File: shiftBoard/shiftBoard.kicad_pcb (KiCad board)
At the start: 2 copper layers, 29 parts, among them J1 Screw_Terminal_01x02, J2 Screw_Terminal_01x02, J3 Screw_Terminal_01x02, J4 Screw_Terminal_01x02, Q1 AO3400A, Q2 AO3400A, Q3 AO3400A, Q4 AO3400A, Q5 AO3400A, Q6 AO3400A, Q7 AO3400A, Q9 AO3400A, U2 74HC595

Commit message: PCB upgade
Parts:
- moved +12V8 51.0 mm to (175.0, 136.5), turned to 90 degrees
- moved +12V7 44.0 mm to (175.0, 33.5), turned to 90 degrees
- moved Q9 39.8 mm to (145.8, 137.6), turned to 0 degrees
- moved D1 37.5 mm to (155.9, 131.5)
- moved +12V1 34.0 mm to (175.0, 121.5), turned to 90 degrees
- moved D8 32.2 mm to (156.8, 27.5), turned to 0 degrees
- moved +12V6 30.5 mm to (175.0, 47.5), turned to 90 degrees
- moved Q7 25.9 mm to (145.8, 35.0), turned to 0 degrees
- moved Q1 20.2 mm to (145.8, 123.0), turned to 0 degrees
- moved D2 17.4 mm to (155.4, 116.0)
- moved D7 12.2 mm to (156.4, 41.5), turned to 0 degrees
- moved D4 11.7 mm to (156.0, 85.5), turned to 0 degrees
- moved D3 11.4 mm to (155.9, 100.5), turned to 0 degrees
- moved D6 11.4 mm to (156.4, 57.0), turned to 0 degrees
- moved Q2 11.0 mm to (145.8, 107.0)
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
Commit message: PCB board
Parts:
- moved J1 28.9 mm to (125.0, 96.5)
- moved J2 22.2 mm to (125.0, 83.0)
- moved Q9 18.2 mm to (157.0, 123.2), turned to 90 degrees
- moved J3 17.4 mm to (125.0, 69.5)
- moved Q1 16.7 mm to (157.0, 110.7), turned to 90 degrees
- moved J4 16.4 mm to (124.7, 51.0)
- moved Q2 14.1 mm to (157.0, 98.5), turned to 90 degrees
- moved +12V8 13.5 mm to (175.5, 123.0)
- moved D1 13.5 mm to (156.4, 118.0)
- moved Q3 12.7 mm to (157.0, 86.7), turned to 90 degrees
- moved Q4 11.8 mm to (157.0, 74.5), turned to 90 degrees
- moved Q7 11.8 mm to (157.0, 38.5), turned to 90 degrees
- moved Q5 11.4 mm to (157.0, 62.2), turned to 90 degrees
- moved Q6 11.3 mm to (157.0, 50.5), turned to 90 degrees
- moved +12V1 10.5 mm to (175.5, 111.0)
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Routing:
- net Net-(+12V1-Pin_2): track 0.00 -> 90.7 mm
- net Net-(U2-QA): track 0.00 -> 56.8 mm
- net Net-(U2-QB): track 0.00 -> 36.6 mm
- net Net-(U2-QH): track 0.00 -> 35.7 mm
- net Net-(U2-QG): track 0.00 -> 26.4 mm
- net Net-(U2-QC): track 0.00 -> 26.3 mm
- net Net-(+12V7-Pin_1): track 0.00 -> 23.6 mm
- net Net-(+12V1-Pin_1): track 0.00 -> 23.6 mm
- net Net-(+12V6-Pin_1): track 0.00 -> 23.5 mm
- net Net-(+12V5-Pin_1): track 0.00 -> 23.4 mm
- net Net-(+12V3-Pin_1): track 0.00 -> 23.3 mm
- net Net-(+12V2-Pin_1): track 0.00 -> 23.2 mm
- net Net-(+12V8-Pin_1): track 0.00 -> 23.1 mm
- net Net-(+12V4-Pin_1): track 0.00 -> 23.0 mm
- net Net-(U2-QF): track 0.00 -> 16.1 mm
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
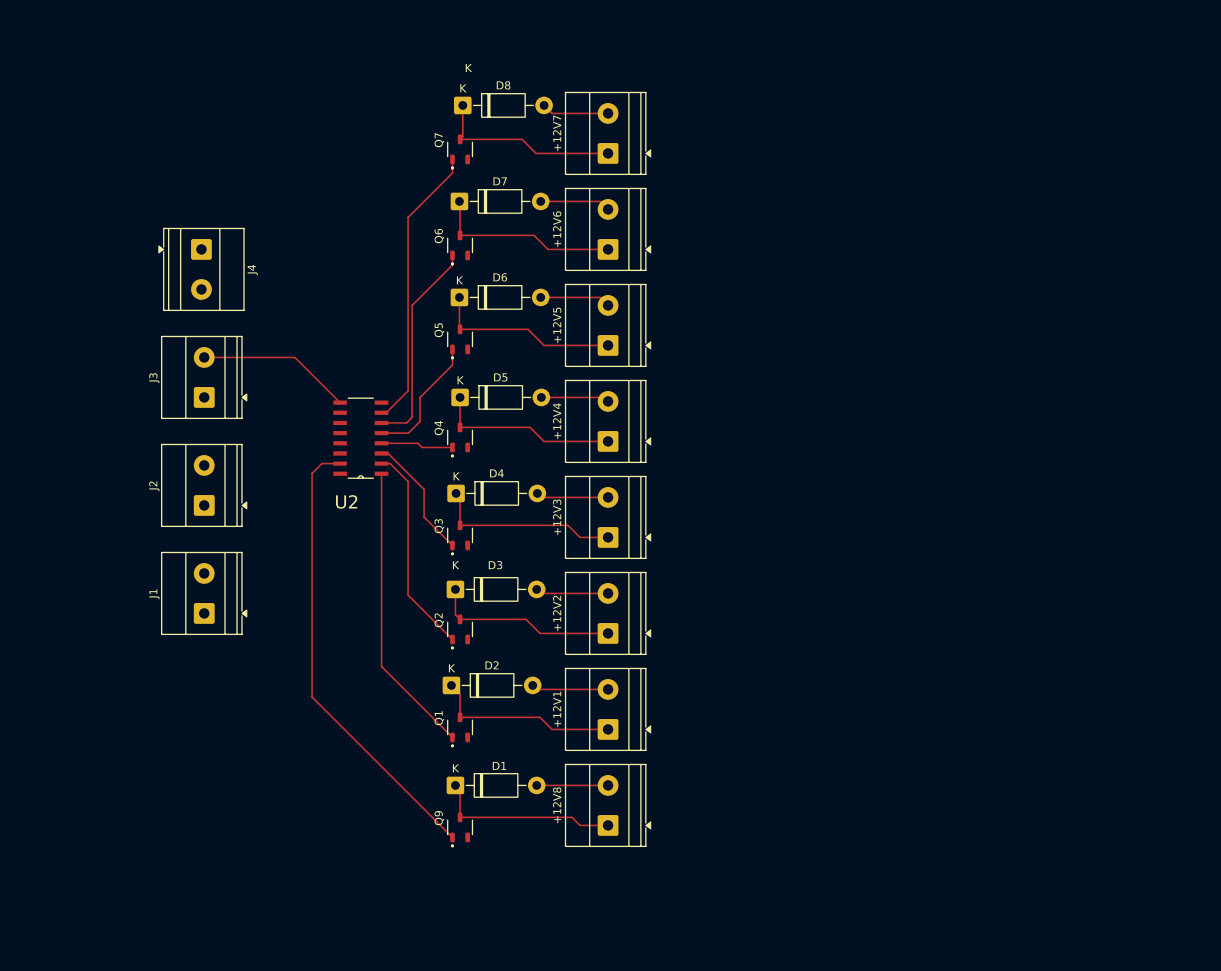
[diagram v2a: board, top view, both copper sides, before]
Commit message: Designed PCB board from scematic
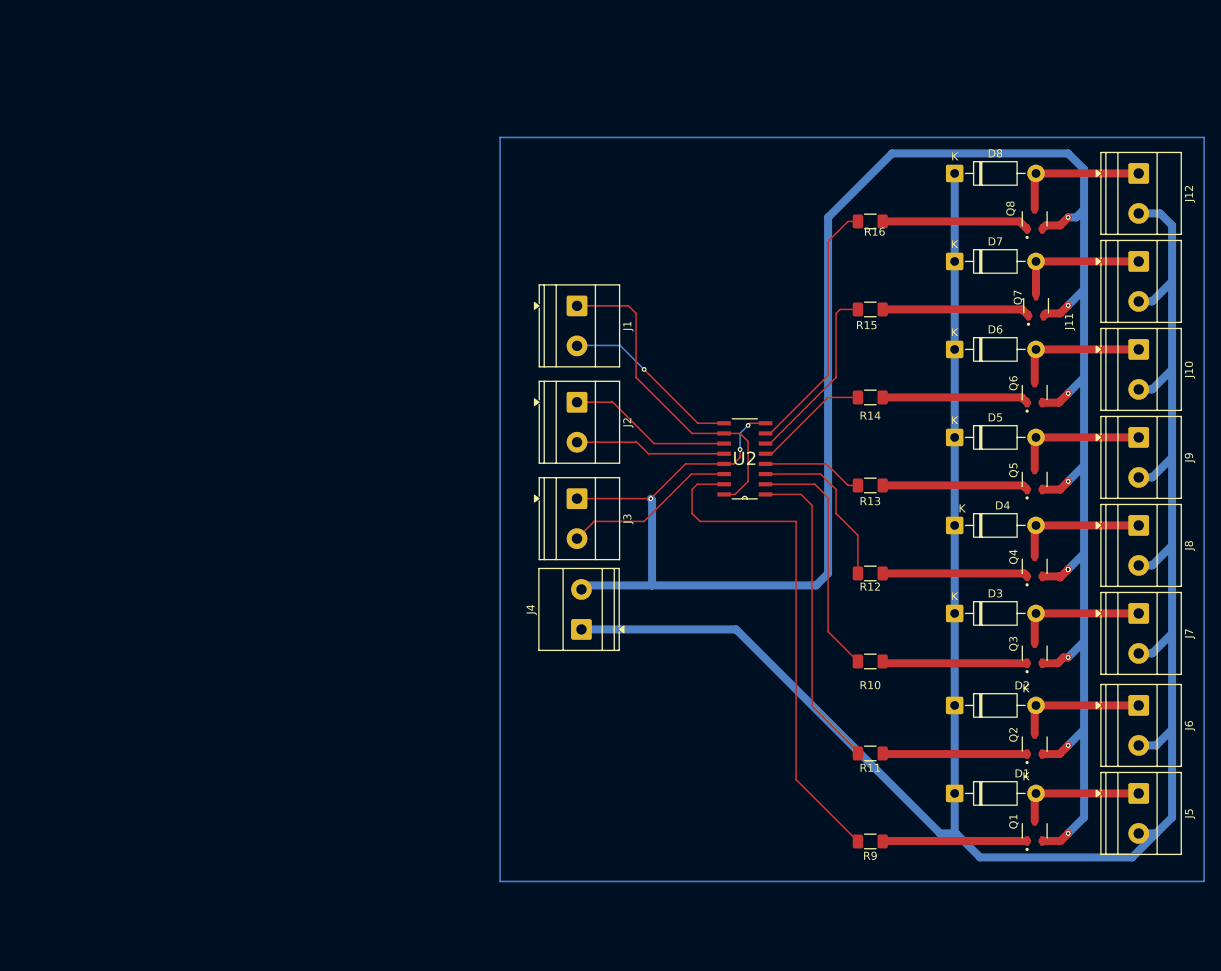
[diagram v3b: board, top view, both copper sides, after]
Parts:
- removed +12V1, +12V2, +12V3, +12V4, +12V5, +12V6, +12V7, +12V8: GND, TerminalBlock_Phoenix:TerminalBlock_Phoenix_MKDS-1,5-2_1x02_P5.00mm_Horizontal
- removed Q9: AO3400A, Library:AO3400A
- added J10: Screw_Terminal_01x02, TerminalBlock_Phoenix:TerminalBlock_Phoenix_MKDS-1,5-2_1x02_P5.00mm_Horizontal, F.Cu at (241.8, 63.5)
- added J11: Screw_Terminal_01x02, TerminalBlock_Phoenix:TerminalBlock_Phoenix_MKDS-1,5-2_1x02_P5.00mm_Horizontal, F.Cu at (241.8, 52.5)
- added J12: Screw_Terminal_01x02, TerminalBlock_Phoenix:TerminalBlock_Phoenix_MKDS-1,5-2_1x02_P5.00mm_Horizontal, F.Cu at (241.8, 41.5)
- added J5: Screw_Terminal_01x02, TerminalBlock_Phoenix:TerminalBlock_Phoenix_MKDS-1,5-2_1x02_P5.00mm_Horizontal, F.Cu at (241.8, 119.0)
- added J6: Screw_Terminal_01x02, TerminalBlock_Phoenix:TerminalBlock_Phoenix_MKDS-1,5-2_1x02_P5.00mm_Horizontal, F.Cu at (241.8, 108.0)
- added J7: Screw_Terminal_01x02, TerminalBlock_Phoenix:TerminalBlock_Phoenix_MKDS-1,5-2_1x02_P5.00mm_Horizontal, F.Cu at (241.8, 96.5)
- added J8: Screw_Terminal_01x02, TerminalBlock_Phoenix:TerminalBlock_Phoenix_MKDS-1,5-2_1x02_P5.00mm_Horizontal, F.Cu at (241.8, 85.5)
- added J9: Screw_Terminal_01x02, TerminalBlock_Phoenix:TerminalBlock_Phoenix_MKDS-1,5-2_1x02_P5.00mm_Horizontal, F.Cu at (241.8, 74.5)
- added Q8: AO3400A, Library:AO3400A, F.Cu at (228.8, 47.2)
- added R10: 100, Resistor_SMD:R_1206_3216Metric_Pad1.30x1.75mm_HandSolder, F.Cu at (208.3, 102.5)
- added R11: 100, Resistor_SMD:R_1206_3216Metric_Pad1.30x1.75mm_HandSolder, F.Cu at (208.3, 114.0)
- added R12: 100, Resistor_SMD:R_1206_3216Metric_Pad1.30x1.75mm_HandSolder, F.Cu at (208.3, 91.5)
- added R13: 100, Resistor_SMD:R_1206_3216Metric_Pad1.30x1.75mm_HandSolder, F.Cu at (208.3, 80.5)
- added R14: 100, Resistor_SMD:R_1206_3216Metric_Pad1.30x1.75mm_HandSolder, F.Cu at (208.3, 69.5)
- added R15: 100, Resistor_SMD:R_1206_3216Metric_Pad1.30x1.75mm_HandSolder, F.Cu at (208.3, 58.5)
- added R16: 100, Resistor_SMD:R_1206_3216Metric_Pad1.30x1.75mm_HandSolder, F.Cu at (208.3, 47.5)
- added R9: 100, Resistor_SMD:R_1206_3216Metric_Pad1.30x1.75mm_HandSolder, F.Cu at (208.3, 125.0)
- moved Q7 74.6 mm to (229.0, 58.0)
- moved Q6 74.1 mm to (228.8, 68.9)
- moved Q5 73.9 mm to (228.8, 79.8)
- moved Q4 73.6 mm to (228.8, 90.6)
- moved Q3 73.3 mm to (228.8, 101.5)
- moved Q2 73.2 mm to (228.8, 112.8)
- moved Q1 73.0 mm to (228.8, 123.7)
- moved J4 67.2 mm to (172.2, 98.5), turned to 90 degrees
- moved D2 63.0 mm to (218.8, 108.0)
- moved D3 62.5 mm to (218.8, 96.5)
- moved D4 62.5 mm to (218.8, 85.5)
- moved D1 62.4 mm to (218.8, 119.0)
- moved D7 62.4 mm to (218.8, 52.5)
- moved D6 62.2 mm to (218.8, 63.5)
- moved D8 62.1 mm to (218.8, 41.5)
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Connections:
- D1 pad 1: Net-(+12V8-Pin_1) -> Net-(D1-K)
- D1 pad 2: Net-(+12V1-Pin_2) -> Net-(D1-A)
- D2 pad 1: Net-(+12V1-Pin_1) -> Net-(D1-K)
- D2 pad 2: Net-(+12V1-Pin_2) -> Net-(D2-A)
- D3 pad 1: Net-(+12V2-Pin_1) -> Net-(D1-K)
- D3 pad 2: Net-(+12V1-Pin_2) -> Net-(D3-A)
- D4 pad 1: Net-(+12V3-Pin_1) -> Net-(D1-K)
- D4 pad 2: Net-(+12V1-Pin_2) -> Net-(D4-A)
- D5 pad 1: Net-(+12V4-Pin_1) -> Net-(D1-K)
- D5 pad 2: Net-(+12V1-Pin_2) -> Net-(D5-A)
- D6 pad 1: Net-(+12V5-Pin_1) -> Net-(D1-K)
- D6 pad 2: Net-(+12V1-Pin_2) -> Net-(D6-A)
- D7 pad 1: Net-(+12V6-Pin_1) -> Net-(D1-K)
- D7 pad 2: Net-(+12V1-Pin_2) -> Net-(D7-A)
- D8 pad 1: Net-(+12V7-Pin_1) -> Net-(D1-K)
- D8 pad 2: Net-(+12V1-Pin_2) -> Net-(D8-A)
- J3 pad 2: Net-(+12V1-Pin_2) -> Net-(J3-Pin_2)
- J4 pad 1: Net-(+12V1-Pin_2) -> Net-(D1-K)
- J4 pad 2: Net-(J4-Pin_2) -> Net-(J3-Pin_1)
- Q1 pad 1: Net-(U2-QB) -> Net-(Q1-Pad1)
- Q1 pad 2: Net-(J4-Pin_2) -> Net-(J3-Pin_1)
- Q1 pad 3: Net-(+12V1-Pin_1) -> Net-(D1-A)
- Q2 pad 1: Net-(U2-QC) -> Net-(Q2-Pad1)
- Q2 pad 2: Net-(J4-Pin_2) -> Net-(J3-Pin_1)
- Q2 pad 3: Net-(+12V2-Pin_1) -> Net-(D2-A)
- Q3 pad 1: Net-(U2-QD) -> Net-(Q3-Pad1)
- Q3 pad 2: Net-(J4-Pin_2) -> Net-(J3-Pin_1)
- Q3 pad 3: Net-(+12V3-Pin_1) -> Net-(D3-A)
- Q4 pad 1: Net-(U2-QE) -> Net-(Q4-Pad1)
- Q4 pad 2: Net-(J4-Pin_2) -> Net-(J3-Pin_1)
- Q4 pad 3: Net-(+12V4-Pin_1) -> Net-(D4-A)
- Q5 pad 1: Net-(U2-QF) -> Net-(Q5-Pad1)
- Q5 pad 2: Net-(J4-Pin_2) -> Net-(J3-Pin_1)
- Q5 pad 3: Net-(+12V5-Pin_1) -> Net-(D5-A)
- Q6 pad 1: Net-(U2-QG) -> Net-(Q6-Pad1)
- Q6 pad 2: Net-(J4-Pin_2) -> Net-(J3-Pin_1)
- Q6 pad 3: Net-(+12V6-Pin_1) -> Net-(D6-A)
- Q7 pad 1: Net-(U2-QH) -> Net-(Q7-Pad1)
- Q7 pad 2: Net-(J4-Pin_2) -> Net-(J3-Pin_1)
- Q7 pad 3: Net-(+12V7-Pin_1) -> Net-(D7-A)
- U2 pad 14: Net-(J1-Pin_2) -> Net-(J3-Pin_2)
- U2 pad 9: Net-(+12V1-Pin_2) -> Net-(J1-Pin_2)
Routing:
- net Net-(J3-Pin_1): track 0.00 -> 284.9 mm, vias 0 -> 12
- net Net-(D1-K): track 0.00 -> 282.3 mm
- net Net-(+12V1-Pin_2): track 90.7 -> 0.00 mm
- net Net-(J1-Pin_1): track 0.00 -> 41.8 mm
- net Net-(+12V7-Pin_1): track 23.6 -> 0.00 mm
- net Net-(+12V1-Pin_1): track 23.6 -> 0.00 mm
- net Net-(+12V6-Pin_1): track 23.5 -> 0.00 mm
- net Net-(+12V5-Pin_1): track 23.4 -> 0.00 mm
- net Net-(+12V3-Pin_1): track 23.3 -> 0.00 mm
- net Net-(+12V2-Pin_1): track 23.2 -> 0.00 mm
- net Net-(+12V8-Pin_1): track 23.1 -> 0.00 mm
- net Net-(+12V4-Pin_1): track 23.0 -> 0.00 mm
- net Net-(J1-Pin_2): track 0.00 -> 22.4 mm, vias 0 -> 1
- net Net-(J3-Pin_2): track 0.00 -> 21.7 mm
- net Net-(J2-Pin_1): track 0.00 -> 20.6 mm
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
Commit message: PCB cut out and errors
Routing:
- net Net-(J3-Pin_1): vias 12 -> 11
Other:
- board outline added: 88 x 93 mm
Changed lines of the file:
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@@
 		(tags "Diode DO-41_SOD81 series Axial Horizontal pin pitch 10.16mm  length 5.2mm diameter 2.7mm")
 		(property "Reference" "D2"
-			(at 8.433809 -2.47 0)
+			(at 5.6725 -2.47 0)
 			(layer "F.SilkS")
 			(effects
@@
 		(tags "Diode DO-41_SOD81 series Axial Horizontal pin pitch 10.16mm  length 5.2mm diameter 2.7mm")
 		(property "Reference" "D1"
-			(at 8.433809 -2.47 0)
+			(at 5.6725 -2.47 0)
 			(layer "F.SilkS")
 			(effects
@@
 		(tags "resistor handsolder")
 		(property "Reference" "R16"
-			(at -0.55 -1.31 0)
+			(at -0.2225 -2 0)
 			(layer "F.SilkS")
 			(effects
@@
 		(stroke
 			(width 0.2)
-			(type default)
+			(type solid)
 		)
 		(fill no)
-		(layer "B.Cu")
+		(layer "Edge.Cuts")
 	)
 	(dimension
@@
 		(size 0.6)
 		(drill 0.3)
-		(layers "F.Cu" "B.Cu")
-		(net 5)
-	)
-	(via
-		(at 233 91)
-		(size 0.6)
-		(drill 0.3)

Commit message: turned a terminal
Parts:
- moved J4 5.05 mm to (171.5, 93.5), turned to -90 degrees
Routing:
- net Net-(D1-K): track 282.3 -> 288.2 mm, vias 0 -> 3
- net Net-(J3-Pin_1): track 284.9 -> 289.4 mm
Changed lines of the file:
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@@
 	(footprint "TerminalBlock_Phoenix:TerminalBlock_Phoenix_MKDS-1,5-2_1x02_P5.00mm_Horizontal"
 		(layer "F.Cu")
-		(at 172.1725 98.5 90)
+		(at 171.5 93.5 -90)
 		(descr "Terminal Block Phoenix MKDS-1,5-2, 2 pins, pitch 5mm, size 10x9.8mm, drill diameter 1.3mm, pad diameter 2.6mm, http://www.farnell.com/datasheets/100425.pdf, script-generated using https://gitlab.com/kicad/libraries/kicad-footprint-generator/-/tree/master/scripts/TerminalBlock_Phoenix")
 		(tags "THT Terminal Block Phoenix MKDS-1,5-2 pitch 5mm size 10x9.8mm drill 1.3mm pad 2.6mm")
@@
 		(attr through_hole)
 		(fp_line
-			(start 7.62 -5.32)
-			(end 7.62 4.72)
+			(start -2.62 4.72)
+			(end -2.62 -5.32)
 			(stroke
 				(width 0.12)
@@
 		)
 		(fp_line
-			(start -2.62 -5.32)
-			(end 7.62 -5.32)
+			(start -0.3 4.72)
+			(end -2.62 4.72)
 			(stroke
 				(width 0.12)
@@
 		)
 		(fp_line
-			(start -2.62 -2.3)
-			(end 7.62 -2.3)
+			(start 7.62 4.72)
+			(end 0.3 4.72)
 			(stroke
 				(width 0.12)
@@
 		)
 		(fp_line
-			(start -2.62 2.6)
-			(end 7.62 2.6)
+			(start -2.62 4.1)
+			(end 7.62 4.1)
 			(stroke
 				(width 0.12)
@@
 		)
 		(fp_line
-			(start -2.62 4.1)
-			(end 7.62 4.1)
+			(start -2.62 2.6)
+			(end 7.62 2.6)
 			(stroke
 				(width 0.12)
@@
 		)
 		(fp_line
-			(start 7.62 4.72)
-			(end 0.3 4.72)
+			(start -2.62 -2.3)
+			(end 7.62 -2.3)
 			(stroke
 				(width 0.12)
@@
 		)
 		(fp_line
-			(start -0.3 4.72)
-			(end -2.62 4.72)
+			(start -2.62 -5.32)
+			(end 7.62 -5.32)
 			(stroke
 				(width 0.12)
@@
 		)
 		(fp_line
-			(start -2.62 4.72)
-			(end -2.62 -5.32)
+			(start 7.62 -5.32)
+			(end 7.62 4.72)
 			(stroke
 				(width 0.12)
@@
 		)
 		(fp_line
-			(start 7.5 -5.2)
-			(end 7.5 4.6)
+			(start -2 4.6)
+			(end -2.5 4.1)
 			(stroke
 				(width 0.1)
@@
 		)
 		(fp_line
-			(start -2.5 -5.2)
-			(end 7.5 -5.2)
+			(start 7.5 4.6)
+			(end -2 4.6)
 			(stroke
 				(width 0.1)
@@
 		)
 		(fp_line
-			(start -2.5 -2.3)
-			(end 7.5 -2.3)
+			(start -2.5 4.1)
+			(end 7.5 4.1)
 			(stroke
 				(width 0.1)
@@
 		)
 		(fp_line
-			(start 5.955 -1.138)
-			(end 3.862 0.955)
+			(start -2.5 4.1)
+			(end -2.5 -5.2)
 			(stroke
 				(width 0.1)
@@
 		)
 		(fp_line
-			(start 0.955 -1.138)
-			(end -1.138 0.955)
+			(start -2.5 2.6)
+			(end 7.5 2.6)
 			(stroke
 				(width 0.1)
@@
 		)
 		(fp_line
-			(start 6.138 -0.955)
-			(end 4.045 1.138)
+			(start 1.138 -0.955)
+			(end -0.955 1.138)
 			(stroke
 				(width 0.1)
@@
 		)
 		(fp_line
-			(start 1.138 -0.955)
-			(end -0.955 1.138)
+			(start 6.138 -0.955)
+			(end 4.045 1.138)
 			(stroke
 				(width 0.1)
@@
 		)
 		(fp_line
-			(start -2.5 2.6)
-			(end 7.5 2.6)
+			(start 0.955 -1.138)
+			(end -1.138 0.955)
 			(stroke
 				(width 0.1)
@@
 		)
 		(fp_line
-			(start -2.5 4.1)
-			(end -2.5 -5.2)
+			(start 5.955 -1.138)
+			(end 3.862 0.955)
 			(stroke
 				(width 0.1)
@@
 		)
 		(fp_line
-			(start -2.5 4.1)
-			(end 7.5 4.1)
+			(start -2.5 -2.3)
+			(end 7.5 -2.3)
 			(stroke
 				(width 0.1)
@@
 		)
 		(fp_line
-			(start 7.5 4.6)
-			(end -2 4.6)
+			(start -2.5 -5.2)
+			(end 7.5 -5.2)
 			(stroke
 				(width 0.1)
@@
 		)
 		(fp_line
-			(start -2 4.6)
-			(end -2.5 4.1)
+			(start 7.5 -5.2)
+			(end 7.5 4.6)
 			(stroke
 				(width 0.1)
@@
 		)
 		(fp_circle
-			(center 5 0)
-			(end 6.5 0)
+			(center 0 0)
+			(end 1.5 0)
 			(stroke
 				(width 0.1)
@@
 		)
 		(fp_circle
-			(center 0 0)
-			(end 1.5 0)
+			(center 5 0)
+			(end 6.5 0)
 			(stroke
 				(width 0.1)
@@
 		)
 		(pad "1" thru_hole roundrect
-			(at 0 0 90)
+			(at 0 0 270)
 			(size 2.6 2.6)
 			(drill 1.3)
@@
 		)
 		(pad "2" thru_hole circle
-			(at 5 0 90)
+			(at 5 0 270)
 			(size 2.6 2.6)
 			(drill 1.3)
@@
 	)
 	(segment
-		(start 181 93)
-		(end 172.6725 93)
-		(width 1)
-		(layer "B.Cu")
-		(net 5)
-	)
-	(segment
 		(start 201.5 93)
 		(end 181 93)
@@
 	)
 	(segment
-		(start 172.6725 93)
-		(end 172.1725 93.5)
-		(width 1)
-		(layer "B.Cu")
-		(net 5)
-	)
-	(segment
 		(start 192 76)
 		(end 192 74)
@@
 	)
 	(segment
+		(start 181 93)
+		(end 181 96)
+		(width 1)
+		(layer "B.Cu")
+		(net 5)
+	)
+	(segment
 		(start 235 78)
 		(end 235 89)
@@
 	)
 	(segment
+		(start 181 96)
+		(end 178.5 98.5)
+		(width 1)
+		(layer "B.Cu")
+		(net 5)
+	)
+	(segment
 		(start 181 93)
 		(end 181 82.305)
@@
 	)
 	(segment
+		(start 178.5 98.5)
+		(end 171.5 98.5)
+		(width 1)
+		(layer "B.Cu")
+		(net 5)
+	)
+	(segment
 		(start 233 113)
 		(end 235 111)
@@
 	)
 	(segment
+		(start 188.5 98.5)
+		(end 189 98.5)
+		(width 1)
+		(layer "F.Cu")
+		(net 14)
+	)
+	(segment
+		(start 186.5 98.5)
+		(end 188.5 98.5)
+		(width 1)
+		(layer "F.Cu")
+		(net 14)
+	)
+	(segment
+		(start 181.5 93.5)
+		(end 171.5 93.5)
+		(width 1)
+		(layer "F.Cu")
+		(net 14)
+	)
+	(segment
+		(start 186.5 98.5)
+		(end 181.5 93.5)
+		(width 1)
+		(layer "F.Cu")
+		(net 14)
+	)
+	(via
+		(at 188.5 98.5)
+		(size 0.6)
+		(drill 0.3)
+		(layers "F.Cu" "B.Cu")
+		(net 14)
+	)
+	(via
+		(at 187.5 98.5)
+		(size 0.6)
+		(drill 0.3)
+		(layers "F.Cu" "B.Cu")
+		(net 14)
+	)
+	(via
+		(at 186.5 98.5)
+		(size 0.6)
+		(drill 0.3)
+		(layers "F.Cu" "B.Cu")
+		(net 14)
+	)
+	(segment
 		(start 244 113)
 		(end 246 111)
@@
 	)
 	(segment
+		(start 172.6725 93)
+		(end 172.1725 93.5)
+		(width 1)
+		(layer "B.Cu")
+		(net 14)
+	)
+	(segment
 		(start 246 88)
 		(end 246 77)
@@
 	)
 	(segment
+		(start 191.5 98.5)
+		(end 188.5 98.5)
+		(width 1)
+		(layer "B.Cu")
+		(net 14)
+	)
+	(segment
 		(start 217 124)
 		(end 191.5 98.5)
@@
 	)
 	(segment
-		(start 191.5 98.5)
-		(end 172.1725 98.5)
+		(start 244.5 46.5)
+		(end 241.8275 46.5)
 		(width 1)
 		(layer "B.Cu")
@@
 	)
 	(segment
-		(start 244.5 46.5)
-		(end 241.8275 46.5)
+		(start 188.5 98.5)
+		(end 186.5 98.5)
 		(width 1)
 		(layer "B.Cu")

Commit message: pcb recemendations
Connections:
- net Net-(D1-K) renamed /12v
- net Net-(J1-Pin_1) renamed /VCC
- net Net-(J1-Pin_2) renamed /DAYISY CHAIN
- net Net-(J3-Pin_1) renamed /GND
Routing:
- net /GND: track 289.4 -> 278.4 mm, vias 11 -> 10
- net /12v: track 288.2 -> 286.0 mm
- added copper zone on F.Cu, net /12v
- added copper zone on B.Cu, net /GND
